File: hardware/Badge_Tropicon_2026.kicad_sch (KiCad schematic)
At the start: 58 parts, among them J1 Battery, J2 LCD, P1 USB_C_Plug_USB2.0, Q1 DMG3415U-7, SW3 ON, U1 ESP32-S3-WROOM-1-N8, U2 BL8072CLTR33, U3 Si4463, U4 AHT30, U5 VGdd79S915N0S1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

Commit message: feat(Hw):Update_Schematic
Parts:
- added Q2: BC846, Package_TO_SOT_SMD:SOT-23, symbol Transistor_BJT:BC846
- added R13: 1K, Resistor_SMD:R_0603_1608Metric, symbol Device:R
- added R14: 3.9r, Resistor_SMD:R_0603_1608Metric, symbol Device:R
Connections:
- net GND: now also Q2.2 (E); no longer J2.8 (Pin_8)
- net LCD_BRIGHT: now reaches U1.38 (IO2)
- net LCD_BRIGHT: now also R13.1
- new net: Q2.3 (C), R14.1
- new net: Q2.1 (B), R13.2
- new net LEDK: J2.8 (Pin_8), R14.2
- no-connect marks 5 -> 8
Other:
- moved on the sheet: J2, R12, R3

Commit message: feat(Hw):Init_Floorplan
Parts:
- Y1: symbol Device:Crystal_Small -> Device:Crystal_GND2
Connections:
- net GND: now also Y1.2, Y1.4
- net IO0: now also U1.35 (IO42); no longer U1.25 (IO48)
- net IO1: now also U1.34 (IO41); no longer U1.26 (IO45)
- net IO2: now also U1.26 (IO45); no longer U1.34 (IO41)
- net IO3: now also U1.25 (IO48); no longer U1.35 (IO42)
- net at Y1.1: now also U3.17 (XIN); no longer U3.16 (XOUT)
- new net: U3.16 (XOUT), Y1.3
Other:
- moved on the sheet: AE2, C15, C16, C17, C19, C20, C22, L1, L3, R6, R7, U3

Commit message: feat(Hw):Update_Schematic
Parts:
- added C23: 9pF, Capacitor_SMD:C_0603_1608Metric, symbol Device:C
- added C24: 8.7pF, Capacitor_SMD:C_0603_1608Metric, symbol Device:C
- added R15: 110r, Capacitor_SMD:C_0603_1608Metric, symbol Device:R
- added R16: 113r, Capacitor_SMD:C_0603_1608Metric, symbol Device:R
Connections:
- net GND: now also C24.2, R15.2
- new net: C24.1, R16.2
- new net: C23.2, R15.1, R16.1
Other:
- moved on the sheet: AE1, AE2, C10, C11, C12, C13, C14, C15, C16, C17, C18, C19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

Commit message: feat(Hw):Update_SI4463_Antenna
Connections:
- net Rxp is gone; now on net GND: C17.2, L1.1, L3.1, U3.2 (RXp)
- net Rxn: now also C23.1; no longer C20.1, L1.2
- net at C24.1, R16.2: now also C20.1, L1.2
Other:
- moved on the sheet: AE2, C17, C20, C22, C23, C24, L1, L3, R10, R11, R15, R16

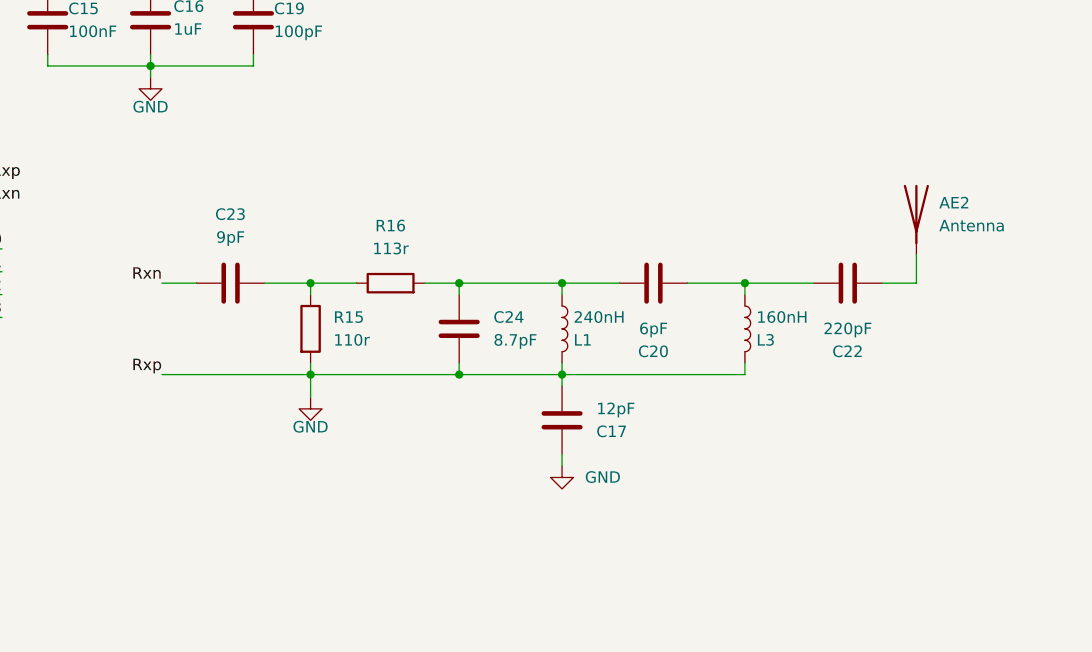
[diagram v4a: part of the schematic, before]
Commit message: Fix: Modify RF filter and DNP
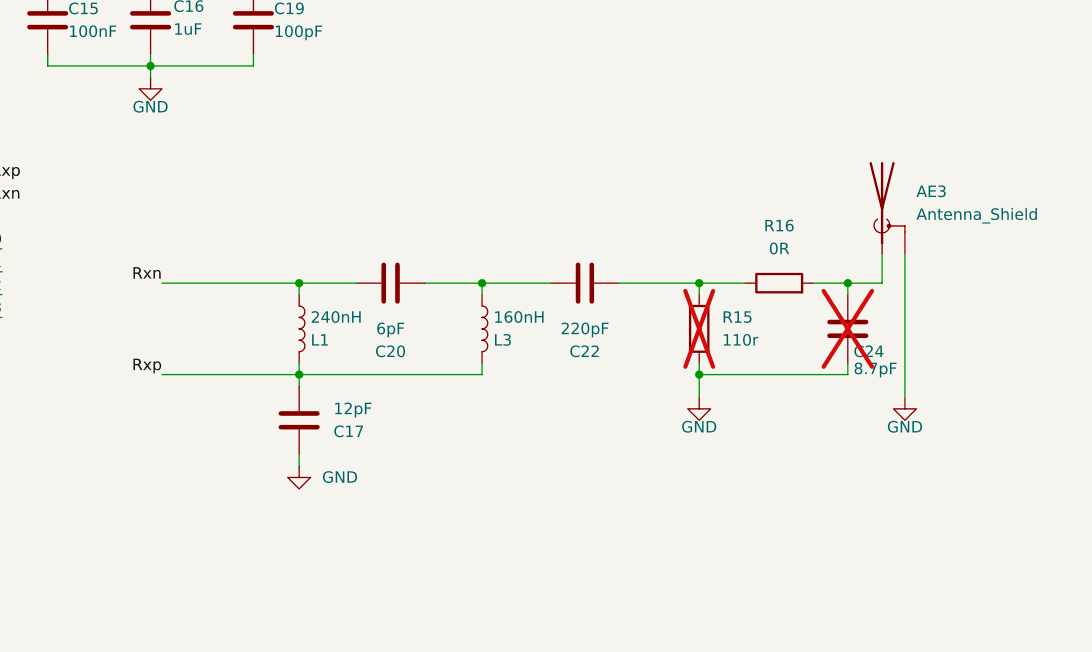
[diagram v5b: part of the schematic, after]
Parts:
- removed AE2: Antenna, Connector_PinHeader_2.54mm:PinHeader_1x01_P2.54mm_Vertical, symbol Device:Antenna
- removed C23: 9pF, Capacitor_SMD:C_0603_1608Metric, symbol Device:C
- added AE3: Antenna_Shield, Connector_PinHeader_2.54mm:PinHeader_1x02_P2.54mm_Vertical, symbol Device:Antenna_Shield
- C24, R15: now not fitted
- R16: value 113r -> 0R; LCSC# C49010135 -> (none)
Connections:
- net GND: now also AE3.2 (Shield); no longer C17.2, L1.1, L3.1, U3.2 (RXp)
- net Rxn: now also C20.1, L1.2
- net at C24.1, R16.2: now also AE3.1 (A); no longer C20.1, L1.2
- net at R15.1, R16.1: now also C22.2
- new net Rxp: C17.2, L1.1, L3.1, U3.2 (RXp)
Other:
- moved on the sheet: C17, C20, C22, L1, L3, R16

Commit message: feat(Hw):Update_Floorplan
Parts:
- J2: LCSC# C2856816 o C262583 -> C262583
- U2: footprint Package_TO_SOT_SMD:SOT-223-3_TabPin2 -> Package_TO_SOT_SMD:SOT-223
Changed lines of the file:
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@@
 			)
 		)
-		(property "Footprint" "Package_TO_SOT_SMD:SOT-223-3_TabPin2"
+		(property "Footprint" "Package_TO_SOT_SMD:SOT-223"
 			(at 189.23 153.67 0)
 			(effects
@@
 			)
 		)
-		(property "LCSC#" "C2856816 o C262583"
+		(property "LCSC#" "C262583"
 			(at 107.95 246.38 0)
 			(effects

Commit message: feat(Hw):Update_Schematic_And_Init_Route
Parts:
- removed C18, C21: 6.8pF, Capacitor_SMD:C_0603_1608Metric, symbol Device:C
- removed L2: 10nH, Inductor_SMD:L_0603_1608Metric, symbol Device:L
- removed R12: 47r, Resistor_SMD:R_0603_1608Metric, symbol Device:R
- added R12: 10K, Resistor_SMD:R_0603_1608Metric, symbol Device:R_Small
- added R17, R18: 4.7K, Resistor_SMD:R_0603_1608Metric, symbol Device:R
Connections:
- net LEDA is gone; now on net +3.3V: J2.9 (Pin_9)
- net +3.3V: now also R12.2, R17.1, R18.1
- net BUSY: now also U1.32 (IO39); no longer U1.16 (IO46)
- net CS0: now also U1.31 (IO38); no longer U1.8 (IO15)
- net CS2: now also U1.22 (IO14); no longer U1.31 (IO38)
- net DIO: now also U1.25 (IO48); no longer U1.4 (IO4)
- net DOWN: now also U1.37 (TXD0); no longer U1.23 (IO21)
- net IO0: now also U1.7 (IO7); no longer U1.35 (IO42)
- net IO1: now also U1.6 (IO6); no longer U1.34 (IO41)
- net IO2: now also U1.5 (IO5); no longer U1.26 (IO45)
- net IRQ: now also U1.12 (IO8); no longer U1.32 (IO39)
- net LEFT: now also U1.39 (IO1); no longer U1.21 (IO13)
- net MISO: now also U1.29 (IO36); no longer U1.10 (IO17)
- net MISO2: now also U1.10 (IO17); no longer U1.29 (IO36)
- net MOSI: now also U1.28 (IO35); no longer U1.9 (IO16)
- net MOSI2: now also U1.9 (IO16); no longer U1.28 (IO35)
- net RIGHT: now also U1.11 (IO18); no longer U1.22 (IO14)
- net RST: now also U1.24 (IO47), R12.1; no longer U1.15 (IO3)
- net RSTB: now also U1.23 (IO21); no longer U1.12 (IO8)
- net SCK: now also U1.30 (IO37); no longer U1.11 (IO18)
- net SCK2: now also U1.8 (IO15); no longer U1.30 (IO37)
- net SCL: now also R18.2
- net SCL1: now also U1.34 (IO41); no longer U1.6 (IO6)
- net SDA: now also R17.2
- net SDA1: now also U1.35 (IO42); no longer U1.5 (IO5)
- net SDN: now also U1.4 (IO4); no longer U1.33 (IO40)
- net TE: now also U1.21 (IO13); no longer U1.7 (IO7)
- net UP: now also U1.33 (IO40); no longer U1.24 (IO47)
- net at AE1.1 (A): now also U5.14 (ANT)
- net IO3: no longer names the net of U3.20 (GPIO3)
- net IO3: no longer U1.25 (IO48)
- no-connect marks 8 -> 10
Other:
- moved on the sheet: AE1, J2, Q2, R13, R14, R16, R3

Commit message: feat(Hw):Update_Route
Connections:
- net IO0: now also U1.6 (IO6); no longer U1.7 (IO7)
- net IO1: now also U1.7 (IO7); no longer U1.6 (IO6)
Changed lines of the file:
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@@
 	)
 	(label "IO1"
-		(at 35.56 45.72 180)
+		(at 35.56 48.26 180)
 		(effects
 			(font
@@
 	)
 	(label "IO0"
-		(at 35.56 48.26 180)
-		(effects
-			(font
+		(at 35.56 45.72 180)
+		(effects
+			(font
